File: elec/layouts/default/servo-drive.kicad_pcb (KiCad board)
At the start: 4 copper layers, 37.6 x 39.9 mm, 136 parts, among them U37 8Mhz

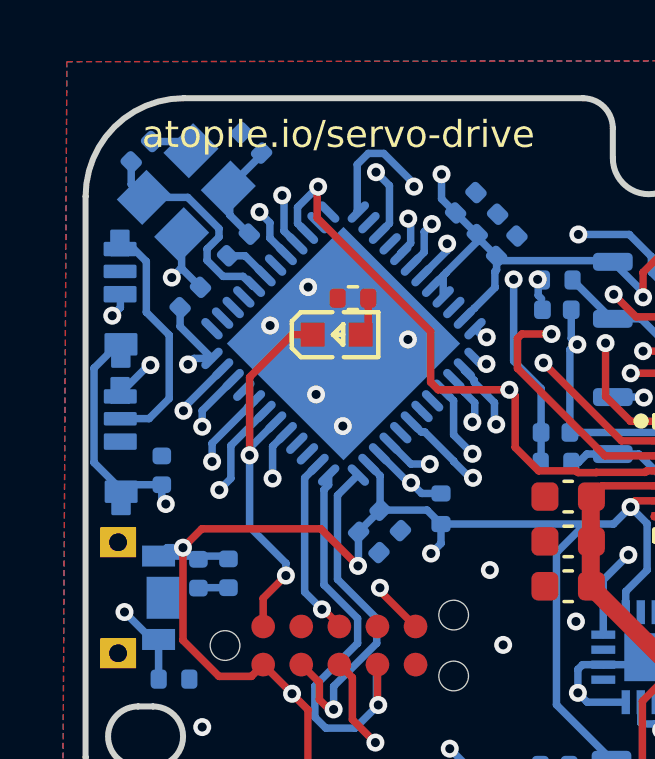
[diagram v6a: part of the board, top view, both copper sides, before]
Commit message: fixing reset pin from PB4(TRST) to PG10_NRST
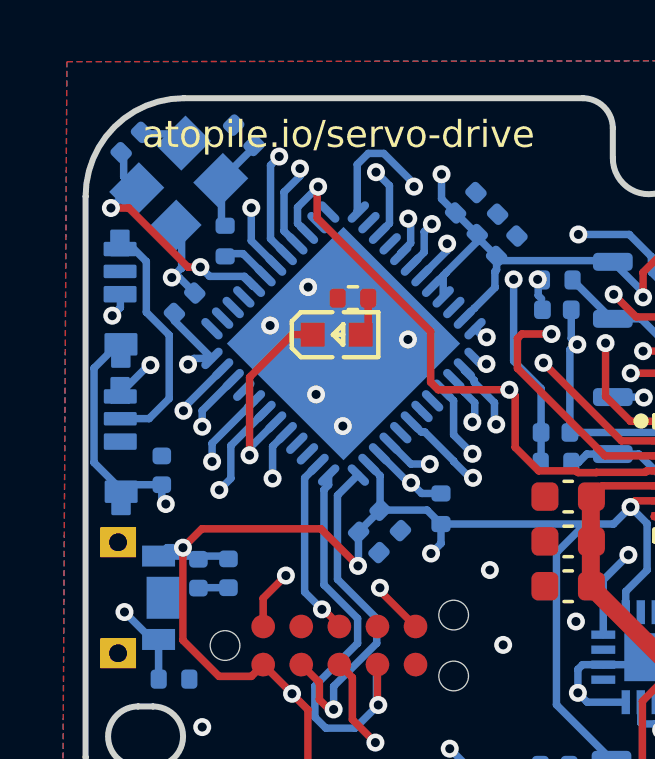
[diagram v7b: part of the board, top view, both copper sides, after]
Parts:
- moved R7 0.46 mm to (209.6, 86.5), turned to 90 degrees
- moved C42 0.45 mm to (206.5, 83.2)
- moved U37 0.36 mm to (208.1, 84.6)
- moved C44 0.36 mm to (210.2, 83.0)
- moved C46 0.27 mm to (208.3, 88.6)
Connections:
- U13 pad 42: micro-reset -> micro-input
- U13 pad 7: micro-PG10_NRST-2 -> micro-PG10_NRST
- U16 pad 10: micro-reset -> micro-PG10_NRST
- U29 pad 1: micro-reset -> micro-input
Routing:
- net micro-PG10_NRST: track 0.00 -> 17.1 mm, vias 0 -> 2
- net micro-reset: track 13.5 -> 0.00 mm, vias 2 -> 0
- net micro-input: track 0.00 -> 6.76 mm, vias 0 -> 1
- net SpinServoNEMA17-PA0: track 25.6 -> 28.7 mm
- net SpinServoNEMA17-in-1: track 30.6 -> 32.4 mm
- net SpinServoNEMA17-INHB: track 30.2 -> 31.9 mm
- net SpinServoNEMA17-data_in: track 17.5 -> 19.2 mm
- net micro-PF0_OSC_IN: track 7.44 -> 8.84 mm, vias 0 -> 2

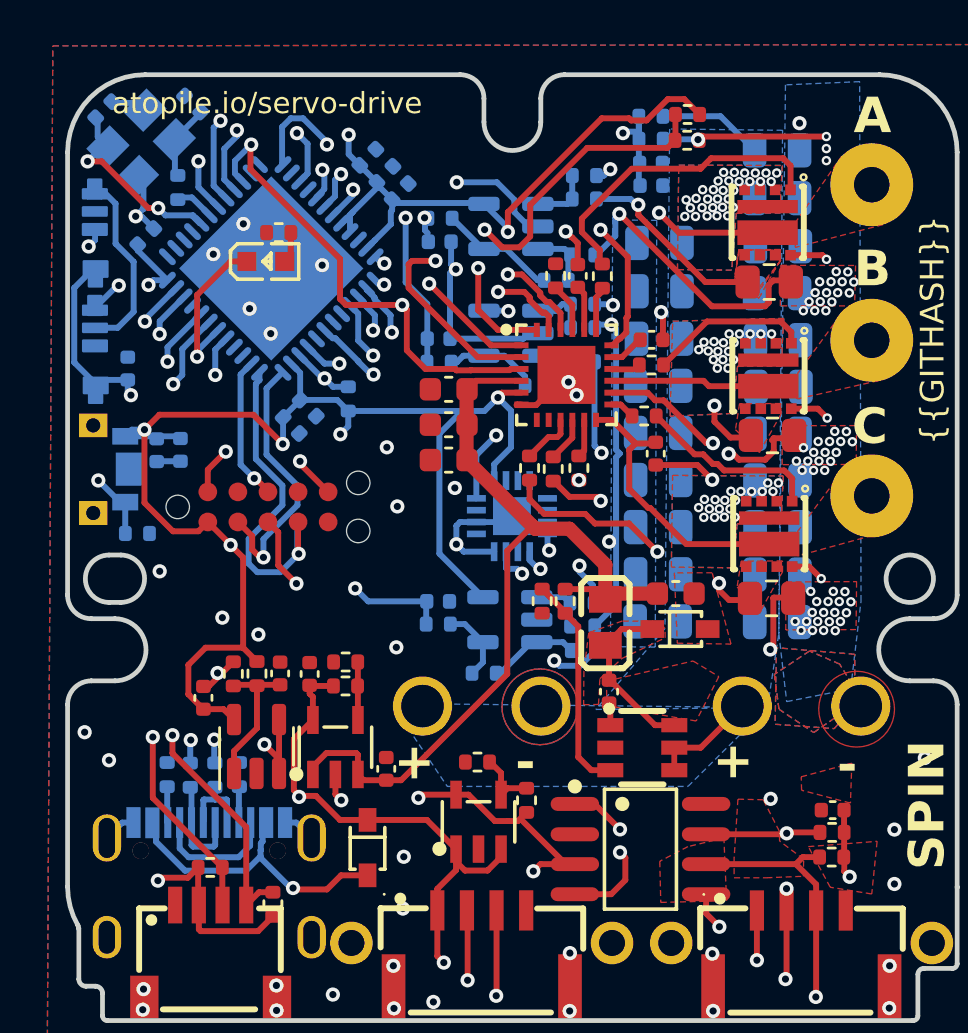
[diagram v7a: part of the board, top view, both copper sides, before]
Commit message: added 100nf caps for current sense opamps
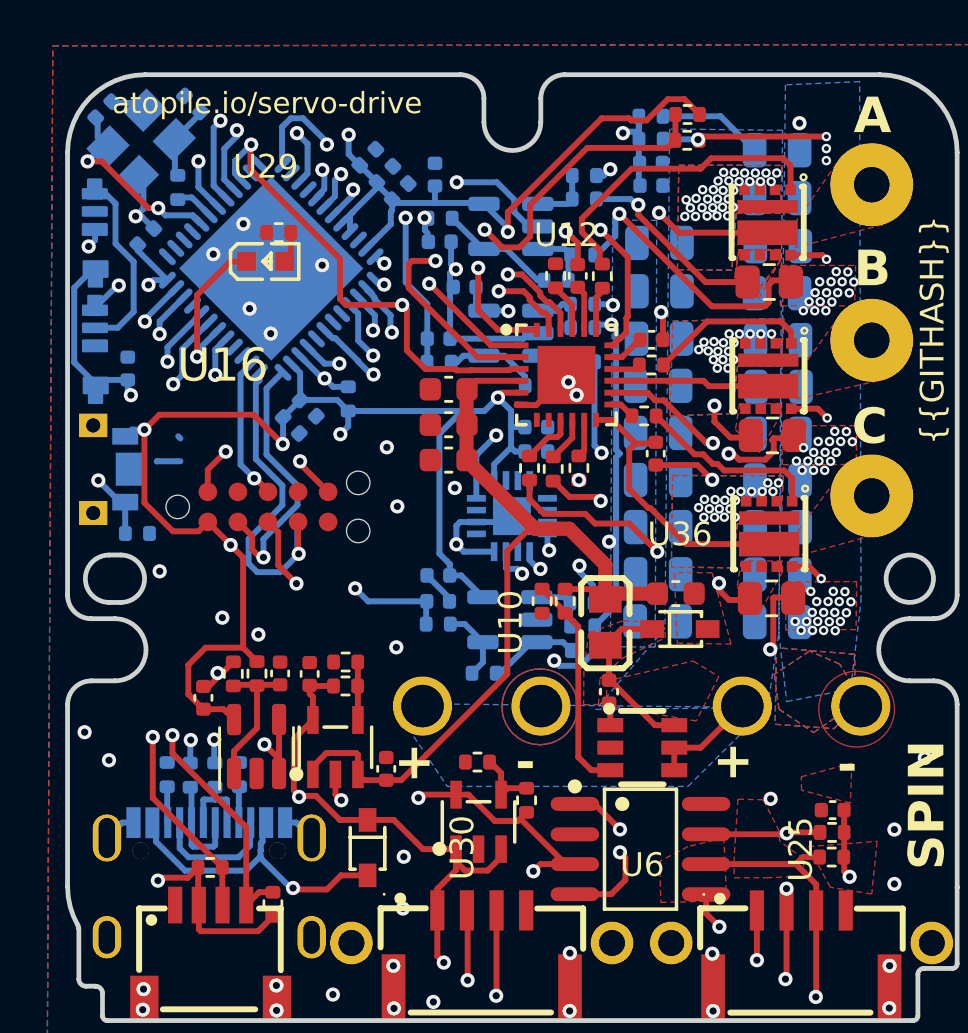
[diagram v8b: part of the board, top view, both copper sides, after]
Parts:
- added C50: 100nF, Capacitor_SMD:C_0402_1005Metric, B.Cu at (221.7, 90.7)
- added C51: 100nF, Capacitor_SMD:C_0402_1005Metric, B.Cu at (220.5, 85.9)
- added C52: 100nF, Capacitor_SMD:C_0402_1005Metric, B.Cu at (224.7, 96.6)
- moved C1 15.0 mm to (224.7, 97.6), turned to 0 degrees
- moved C19 13.0 mm to (220.6, 102.9), turned to 180 degrees
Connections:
- net SpinServoNEMA17-INHB renamed SpinServoNEMA17-phase_b
- net SpinServoNEMA17-INHC renamed SpinServoNEMA17-phase_c
- net SpinServoNEMA17-PA0 renamed SpinServoNEMA17-phase_a
- net SpinServoNEMA17-data_in renamed SpinServoNEMA17-led_pixel
- net SpinServoNEMA17-out-1 renamed SpinServoNEMA17-vin_sense
- net SpinServoNEMA17-vcc renamed SpinServoNEMA17-p1
- net _a-gnd renamed _a-gnd-2
- net _b-i_in-1 renamed _b-i_in-2
- net _c-i_in renamed _c-i_in-2
- net _i_sense-gnd renamed _i_sense-in-5
- net _i_sense-in-6 renamed _i_sense-in-4
- net _i_sense-in_n-7 renamed _i_sense-in_n-5
- net _i_sense-in_n-8 renamed _i_sense-output-8
- net _i_sense-output-4 renamed _i_sense-in_p-3
- net _i_sense-p1-6 renamed _i_sense-input-14
- net gate_reg-fb-1 renamed gate_reg-fb
- net ldo_3v3-adj renamed ldo_3v3-adj-1
- net ldo_5v-adj-1 renamed ldo_5v-output
- net micro-PF0_OSC_IN renamed micro-in
- net micro-PG10_NRST renamed micro-rst
- net micro-can_rx renamed micro-rx
- net micro-can_tx renamed micro-tx
- net micro-input renamed micro-PB4
- net micro-tck-1 renamed micro-tck
- net micro-tdo renamed micro-tdo-1
- net micro-tms-1 renamed micro-PA13-1
- net power_stage-BSTA-1 renamed power_stage-BSTA
- net power_stage-bs-2 renamed power_stage-bs-1
- net power_stage-bs-3 renamed power_stage-BSTB-1
- C1 pad 1: SpinServoNEMA17-out -> SpinServoNEMA17-vin
- C13 pad 1: SpinServoNEMA17-out -> SpinServoNEMA17-vin
- C14 pad 1: SpinServoNEMA17-out -> SpinServoNEMA17-vin
- C15 pad 1: SpinServoNEMA17-out -> SpinServoNEMA17-vin
- C17 pad 1: SpinServoNEMA17-out -> SpinServoNEMA17-vin
- C19 pad 1: SpinServoNEMA17-out -> SpinServoNEMA17-vin
- C20 pad 1: SpinServoNEMA17-in -> SpinServoNEMA17-vin-2
- C21 pad 1: SpinServoNEMA17-in -> SpinServoNEMA17-vin-2
- C22 pad 1: SpinServoNEMA17-in -> SpinServoNEMA17-vin-2
- C23 pad 1: SpinServoNEMA17-vin -> SpinServoNEMA17-vin-1
- C25 pad 1: SpinServoNEMA17-in -> SpinServoNEMA17-vin-2
- C26 pad 1: SpinServoNEMA17-in -> SpinServoNEMA17-vin-2
- C27 pad 1: SpinServoNEMA17-in -> SpinServoNEMA17-vin-2
- C28 pad 1: SpinServoNEMA17-in -> SpinServoNEMA17-vin-2
- C29 pad 1: SpinServoNEMA17-in -> SpinServoNEMA17-vin-2
- C3 pad 1: SpinServoNEMA17-in -> SpinServoNEMA17-vin-2
- C30 pad 1: SpinServoNEMA17-in -> SpinServoNEMA17-vin-2
- C31 pad 1: SpinServoNEMA17-vin -> SpinServoNEMA17-vin-1
- C32 pad 1: SpinServoNEMA17-vin -> SpinServoNEMA17-vin-1
- C35 pad 1: SpinServoNEMA17-in -> SpinServoNEMA17-vin-2
- C36 pad 1: SpinServoNEMA17-in -> SpinServoNEMA17-vin-2
- C37 pad 1: SpinServoNEMA17-in -> SpinServoNEMA17-vin-2
- C38 pad 1: SpinServoNEMA17-in -> SpinServoNEMA17-vin-2
- C39 pad 1: SpinServoNEMA17-in -> SpinServoNEMA17-vin-2
- C4 pad 1: SpinServoNEMA17-in -> SpinServoNEMA17-vin-2
- C40 pad 1: SpinServoNEMA17-out -> SpinServoNEMA17-vin
- C46 pad 1: SpinServoNEMA17-out -> SpinServoNEMA17-vin
- C47 pad 1: SpinServoNEMA17-in -> SpinServoNEMA17-vin-2
- C48 pad 1: SpinServoNEMA17-in -> SpinServoNEMA17-vin-2
- C49 pad 1: SpinServoNEMA17-in -> SpinServoNEMA17-vin-2
- C5 pad 1: SpinServoNEMA17-vin -> SpinServoNEMA17-vin-1
- C6 pad 1: SpinServoNEMA17-in -> SpinServoNEMA17-vin-2
- C7 pad 1: SpinServoNEMA17-out -> SpinServoNEMA17-vin
- C8 pad 1: SpinServoNEMA17-vin -> SpinServoNEMA17-vin-1
- R1 pad 1: SpinServoNEMA17-out -> SpinServoNEMA17-vin
- R11 pad 2: SpinServoNEMA17-out -> SpinServoNEMA17-vin
- R2 pad 1: SpinServoNEMA17-out -> SpinServoNEMA17-vin
- R21 pad 1: SpinServoNEMA17-out -> SpinServoNEMA17-vin
- R25 pad 1: _i_sense-p1-5 -> _i_sense-input-12
- R25 pad 2: _i_sense-output-6 -> _i_sense-in_n-6
- R26 pad 1: _i_sense-output-6 -> _i_sense-in_n-6
- R27 pad 1: SpinServoNEMA17-in -> SpinServoNEMA17-vin-2
- R29 pad 1: SpinServoNEMA17-vin -> SpinServoNEMA17-vin-1
- R3 pad 2: SpinServoNEMA17-in-1 -> SpinServoNEMA17-in
- R39 pad 2: SpinServoNEMA17-out -> SpinServoNEMA17-vin
- R40 pad 2: SpinServoNEMA17-out -> SpinServoNEMA17-vin
- R44 pad 1: _i_sense-input-11 -> _i_sense-p1-4
- R44 pad 2: _i_sense-output-5 -> _i_sense-output-6
- R45 pad 1: _i_sense-output-5 -> _i_sense-output-6
- R50 pad 1: _i_sense-input-12 -> _i_sense-input-13
- R6 pad 1: _i_sense-p1-4 -> _i_sense-input-11
- U1 pad 10: SpinServoNEMA17-in -> SpinServoNEMA17-vin-2
- U1 pad 2: SpinServoNEMA17-in -> SpinServoNEMA17-vin-2
- U1 pad 3: SpinServoNEMA17-in -> SpinServoNEMA17-vin-2
- U1 pad 4: SpinServoNEMA17-in -> SpinServoNEMA17-vin-2
- U10 pad 2: SpinServoNEMA17-vin -> SpinServoNEMA17-vin-1
- U11 pad 1: SpinServoNEMA17-in-1 -> SpinServoNEMA17-in
- U11 pad 2: SpinServoNEMA17-out -> SpinServoNEMA17-vin
- U12 pad 4: SpinServoNEMA17-vin -> SpinServoNEMA17-vin-1
- U12 pad 5: SpinServoNEMA17-out -> SpinServoNEMA17-vin
- U13 pad 13: SpinServoNEMA17-in-1 -> SpinServoNEMA17-in
- U13 pad 20: SpinServoNEMA17-out -> SpinServoNEMA17-vin
- U13 pad 21: SpinServoNEMA17-out -> SpinServoNEMA17-vin
- U13 pad 23: SpinServoNEMA17-out -> SpinServoNEMA17-vin
- U13 pad 35: SpinServoNEMA17-out -> SpinServoNEMA17-vin
- U13 pad 48: SpinServoNEMA17-out -> SpinServoNEMA17-vin
- U14 pad 2: SpinServoNEMA17-in -> SpinServoNEMA17-vin-2
- U15 pad 2: SpinServoNEMA17-out -> SpinServoNEMA17-vin
- U16 pad 1: SpinServoNEMA17-out -> SpinServoNEMA17-vin
- U18 pad 13: SpinServoNEMA17-out -> SpinServoNEMA17-vin
- U19 pad 1: _i_sense-p1-4 -> _i_sense-input-11
- U2 pad 2: SpinServoNEMA17-in -> SpinServoNEMA17-vin-2
- U20 pad 5: SpinServoNEMA17-out -> SpinServoNEMA17-vin
- U21 pad 1: _i_sense-output-5 -> _i_sense-output-6
- U21 pad 3: _i_sense-output-6 -> _i_sense-in_n-6
- U21 pad 5: SpinServoNEMA17-out -> SpinServoNEMA17-vin
- U22 pad 1: SpinServoNEMA17-vin -> SpinServoNEMA17-vin-1
- U22 pad 3: SpinServoNEMA17-vin -> SpinServoNEMA17-vin-1
- U23 pad 5: SpinServoNEMA17-out -> SpinServoNEMA17-vin
- U24 pad 5: SpinServoNEMA17-out -> SpinServoNEMA17-vin
- U25 pad 3: SpinServoNEMA17-out -> SpinServoNEMA17-vin
- U28 pad 10: SpinServoNEMA17-in -> SpinServoNEMA17-vin-2
- U28 pad 2: SpinServoNEMA17-in -> SpinServoNEMA17-vin-2
- U28 pad 3: SpinServoNEMA17-in -> SpinServoNEMA17-vin-2
- U28 pad 4: SpinServoNEMA17-in -> SpinServoNEMA17-vin-2
- U3 pad 10: SpinServoNEMA17-in -> SpinServoNEMA17-vin-2
- U3 pad 2: SpinServoNEMA17-in -> SpinServoNEMA17-vin-2
- U3 pad 3: SpinServoNEMA17-in -> SpinServoNEMA17-vin-2
- U3 pad 4: SpinServoNEMA17-in -> SpinServoNEMA17-vin-2
- U31 pad 1: _i_sense-input-11 -> _i_sense-p1-4
- U33 pad 1: _i_sense-p1-5 -> _i_sense-input-12
- U34 pad 1: _i_sense-input-12 -> _i_sense-input-13
- U4 pad 5: SpinServoNEMA17-out -> SpinServoNEMA17-vin
- U6 pad 4: SpinServoNEMA17-in -> SpinServoNEMA17-vin-2
- U6 pad 5: SpinServoNEMA17-in -> SpinServoNEMA17-vin-2
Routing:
- net SpinServoNEMA17-out: track 113.6 -> 0.13 mm, vias 12 -> 0
- net SpinServoNEMA17-vin: track 37.1 -> 114.6 mm, vias 0 -> 13
- net SpinServoNEMA17-vin-1: track 0.00 -> 37.1 mm
- net SpinServoNEMA17-in-1: track 32.4 -> 0.00 mm, vias 2 -> 0
- net SpinServoNEMA17-in: track 9.01 -> 32.4 mm, vias 68 -> 2
- net _i_sense-p1-5: track 12.3 -> 0.00 mm, vias 2 -> 0
- net SpinServoNEMA17-vin-2: track 0.00 -> 9.01 mm, vias 0 -> 68
- net _i_sense-input-13: track 0.00 -> 8.91 mm, vias 0 -> 2
- net _i_sense-input-12: track 8.91 -> 12.3 mm
- net _i_sense-in_n-6: track 0.00 -> 2.94 mm
- net _i_sense-p1-4: track 11.5 -> 8.98 mm, vias 1 -> 2
- net _i_sense-input-11: track 8.98 -> 11.5 mm, vias 2 -> 1
- net _i_sense-output-5: track 2.49 -> 0.00 mm
- net SpinServoNEMA17-gnd: track 43.1 -> 44.5 mm, vias 102 -> 101
- added copper zone on In2.Cu, net SpinServoNEMA17-vin
- added copper zone on B.Cu, net SpinServoNEMA17-vin-2
- added copper zone on F.Cu, net SpinServoNEMA17-vin-2
- added copper zone on In1.Cu, net SpinServoNEMA17-vin-2
- added copper zone on In2.Cu, net SpinServoNEMA17-vin-2
- removed copper zone on B.Cu, net SpinServoNEMA17-in
- removed copper zone on F.Cu, net SpinServoNEMA17-in
- removed copper zone on In1.Cu, net SpinServoNEMA17-in
- removed copper zone on In2.Cu, net SpinServoNEMA17-in
- removed copper zone on In2.Cu, net SpinServoNEMA17-out
